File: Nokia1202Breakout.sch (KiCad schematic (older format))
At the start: 6 parts, among them J1 Conn_01x08_Male

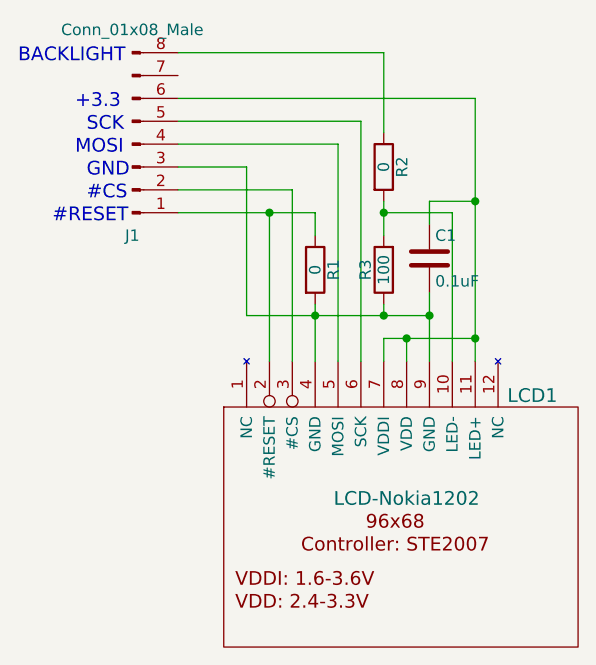
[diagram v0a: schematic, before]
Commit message: Fixed incorrect reset connection.
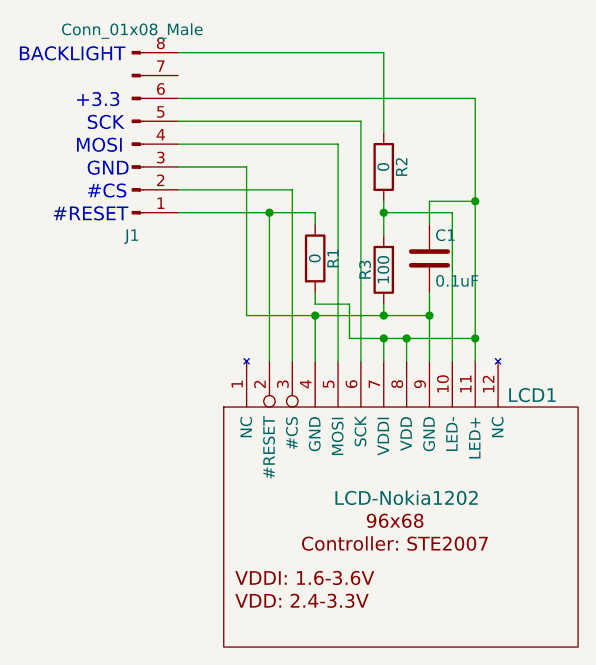
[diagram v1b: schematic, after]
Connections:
- net at C1.1, J1.6 (Pin_6), LCD1.11 (LED+)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: now also R1.2
- net at C1.2, J1.3 (Pin_3), LCD1.4 (GND)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: no longer R1.2
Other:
- moved on the sheet: R1
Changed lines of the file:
@@
 	2200 2100 2200 2000
 Wire Wire Line
-	2200 2000 2600 2000
+	2050 2000 2600 2000
 Wire Wire Line
 	2300 2100 2300 2000
@@
 Wire Wire Line
 	1600 1900 2400 1900
-Wire Wire Line
-	1900 1850 1900 2100
 Connection ~ 2400 1900
 Wire Wire Line
@@
 L R R1
 U 1 1 5A3EAD49
-P 1900 1700
-F 0 "R1" V 1980 1700 50  0000 C CNN
-F 1 "0" V 1900 1700 50  0000 C CNN
-F 2 "Resistors_SMD:R_0805" V 1830 1700 50  0001 C CNN
-F 3 "" H 1900 1700 50  0001 C CNN
-	1    1900 1700
+P 1900 1650
+F 0 "R1" V 1980 1650 50  0000 C CNN
+F 1 "0" V 1900 1650 50  0000 C CNN
+F 2 "Resistors_SMD:R_0805" V 1830 1650 50  0001 C CNN
+F 3 "" H 1900 1650 50  0001 C CNN
+	1    1900 1650
 	1    0    0    -1
 $EndComp
 Connection ~ 1900 1900
-Wire Wire Line
-	1900 1450 1900 1550
-Wire Wire Line
-	1300 1450 1900 1450
 Wire Wire Line
 	1700 1450 1700 2100
@@
 Wire Wire Line
 	2600 950  2600 2100
+Wire Wire Line
+	1900 2100 1900 1900
+Wire Wire Line
+	1900 1850 2050 1850
+Wire Wire Line
+	2050 1850 2050 2000
+Connection ~ 2200 2000
+Wire Wire Line
+	1300 1450 1900 1450
+Wire Wire Line
+	1900 1800 1900 1850
+Wire Wire Line
+	1900 1450 1900 1500
 $EndSCHEMATC

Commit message: Added mounting holes, prepared negative copies for photochemical printing.
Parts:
- J1: footprint Pin_Headers:Pin_Header_Straight_1x08_Pitch2.54mm -> Pin_Headers:Pin_Header_Angled_1x08_Pitch2.54mm
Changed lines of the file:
@@
-$EndComp
-$Comp
-L Conn_01x08_Male J1
-U 1 1 5A3EA674
-P 1100 1150
-F 0 "J1" H 1100 1550 50  0000 C CNN
-F 1 "Conn_01x08_Male" H 1100 650 50  0000 C CNN
-F 2 "Pin_Headers:Pin_Header_Straight_1x08_Pitch2.54mm" H 1100 1150 50  0001 C CNN
-F 3 "" H 1100 1150 50  0001 C CNN
-	1    1100 1150
-	1    0    0    1
 $EndComp
 $Comp
@@
 Wire Wire Line
 	1900 1450 1900 1500
+$Comp
+L Conn_01x08_Male J1
+U 1 1 5A3EA674
+P 1100 1150
+F 0 "J1" H 1100 1550 50  0000 C CNN
+F 1 "Conn_01x08_Male" H 1100 650 50  0000 C CNN
+F 2 "Pin_Headers:Pin_Header_Angled_1x08_Pitch2.54mm" H 1100 1150 50  0001 C CNN
+F 3 "" H 1100 1150 50  0001 C CNN
+	1    1100 1150
+	1    0    0    1
+$EndComp
 $EndSCHEMATC
